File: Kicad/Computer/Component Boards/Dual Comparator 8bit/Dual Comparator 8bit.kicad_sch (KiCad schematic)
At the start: 12 parts, among them IC1 SN74F521NSR, IC2 74LVC16373ADL,118, IC3 SN74F521NSR, IC5 AP7365-33WG-7, J2 Conn_02x20_Counter_Clockwise

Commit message: Routed (mostly) the Dual 8bit comparator.
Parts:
- removed C5: 1μF, SamacSys_Parts:C_0805, symbol HCP65:C_0805
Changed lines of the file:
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@@
     (effects (font (size 1.27 1.27)) (justify right bottom))
-  )
-  (label "GND" (at 168.91 154.305 0) (fields_autoplaced)
-    (effects (font (size 1.27 1.27)) (justify left bottom))
   )
   (label "GND" (at 104.14 113.665 180) (fields_autoplaced)
@@
   )
   (label "D5" (at 40.64 130.81 180) (fields_autoplaced)
-    (effects (font (size 1.27 1.27)) (justify right bottom))
-  )
-  (label "3.3V" (at 163.83 154.305 180) (fields_autoplaced)
     (effects (font (size 1.27 1.27)) (justify right bottom))
   )
@@
         )
       )
-      (project "Pico Sound"
-        (path "/36ae9fab-3bd5-422b-bccc-b7d474dd236c"
-          (reference "C23") (unit 1)
-        )
-      )
-      (project "Video Timer"
-        (path "/5ce90b85-49a2-4937-86c7-662b0d6f8431"
-          (reference "C?") (unit 1)
-        )
-        (path "/5ce90b85-49a2-4937-86c7-662b0d6f8431/662feba9-2017-4e89-b774-f7d895f327d7"
-          (reference "C42") (unit 1)
-        )
-      )
-      (project "Sound"
-        (path "/8357857d-ab8c-4646-b786-aad4001c0a6b/f77e925c-a0a2-46fc-a442-a4077818f930"
-          (reference "C52") (unit 1)
-        )
-      )
-    )
-  )
-  (symbol (lib_id "HCP65:C_0805") (at 163.83 154.305 0) (unit 1)
-    (in_bom yes) (on_board yes) (dnp no)
-    (property "Reference" "C5" (at 166.116 151.765 0)
-      (effects (font (size 1.27 1.27)))
-    )
-    (property "Value" "1μF" (at 166.37 156.845 0)
-      (effects (font (size 1.27 1.27)))
-    )
-    (property "Footprint" "SamacSys_Parts:C_0805" (at 180.594 161.925 0)
-      (effects (font (size 1.27 1.27)) hide)
-    )
-    (property "Datasheet" "" (at 166.0525 153.9875 90)
-      (effects (font (size 1.27 1.27)) hide)
-    )
-    (pin "1")
-    (pin "2")
-    (instances
-      (project "Dual Comparator 8bit"
-        (path "/337b5f72-8be1-4121-9dc6-479b565482b2"
-          (reference "C5") (unit 1)
-        )
-      )

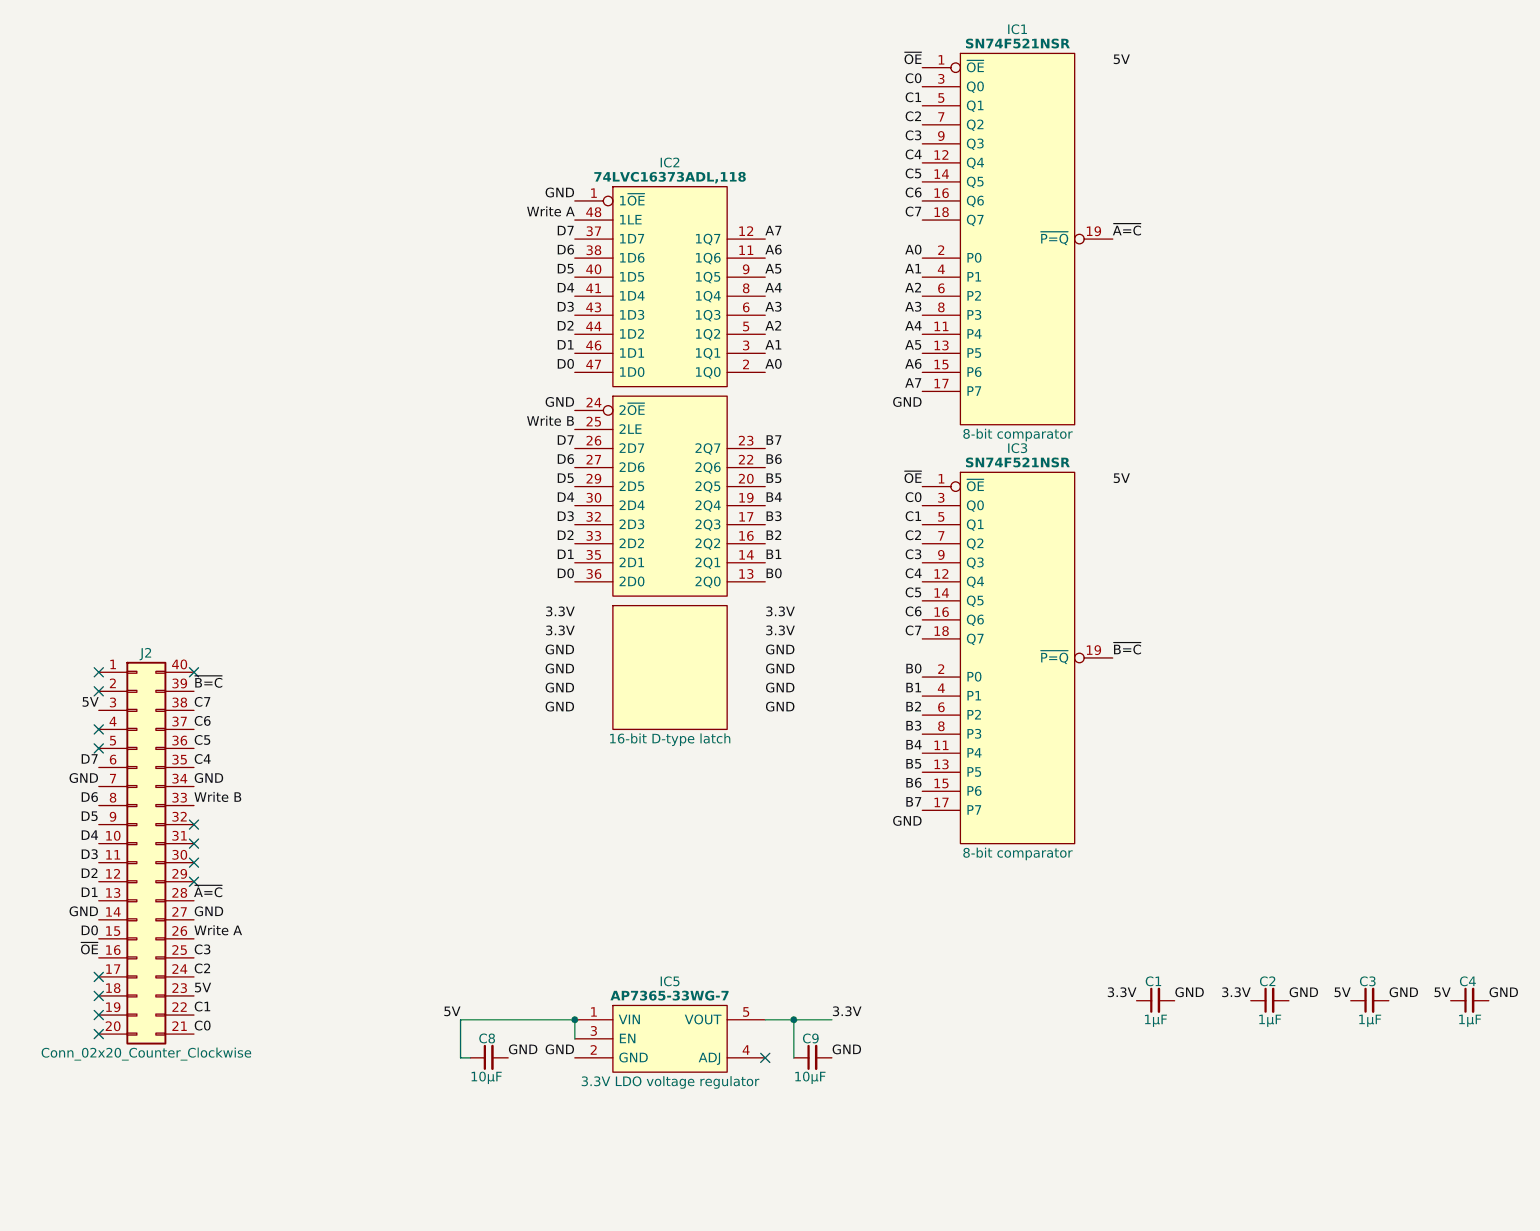
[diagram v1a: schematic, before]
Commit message: Added terminal count output and latch enable to 16bit and 24bit counters.
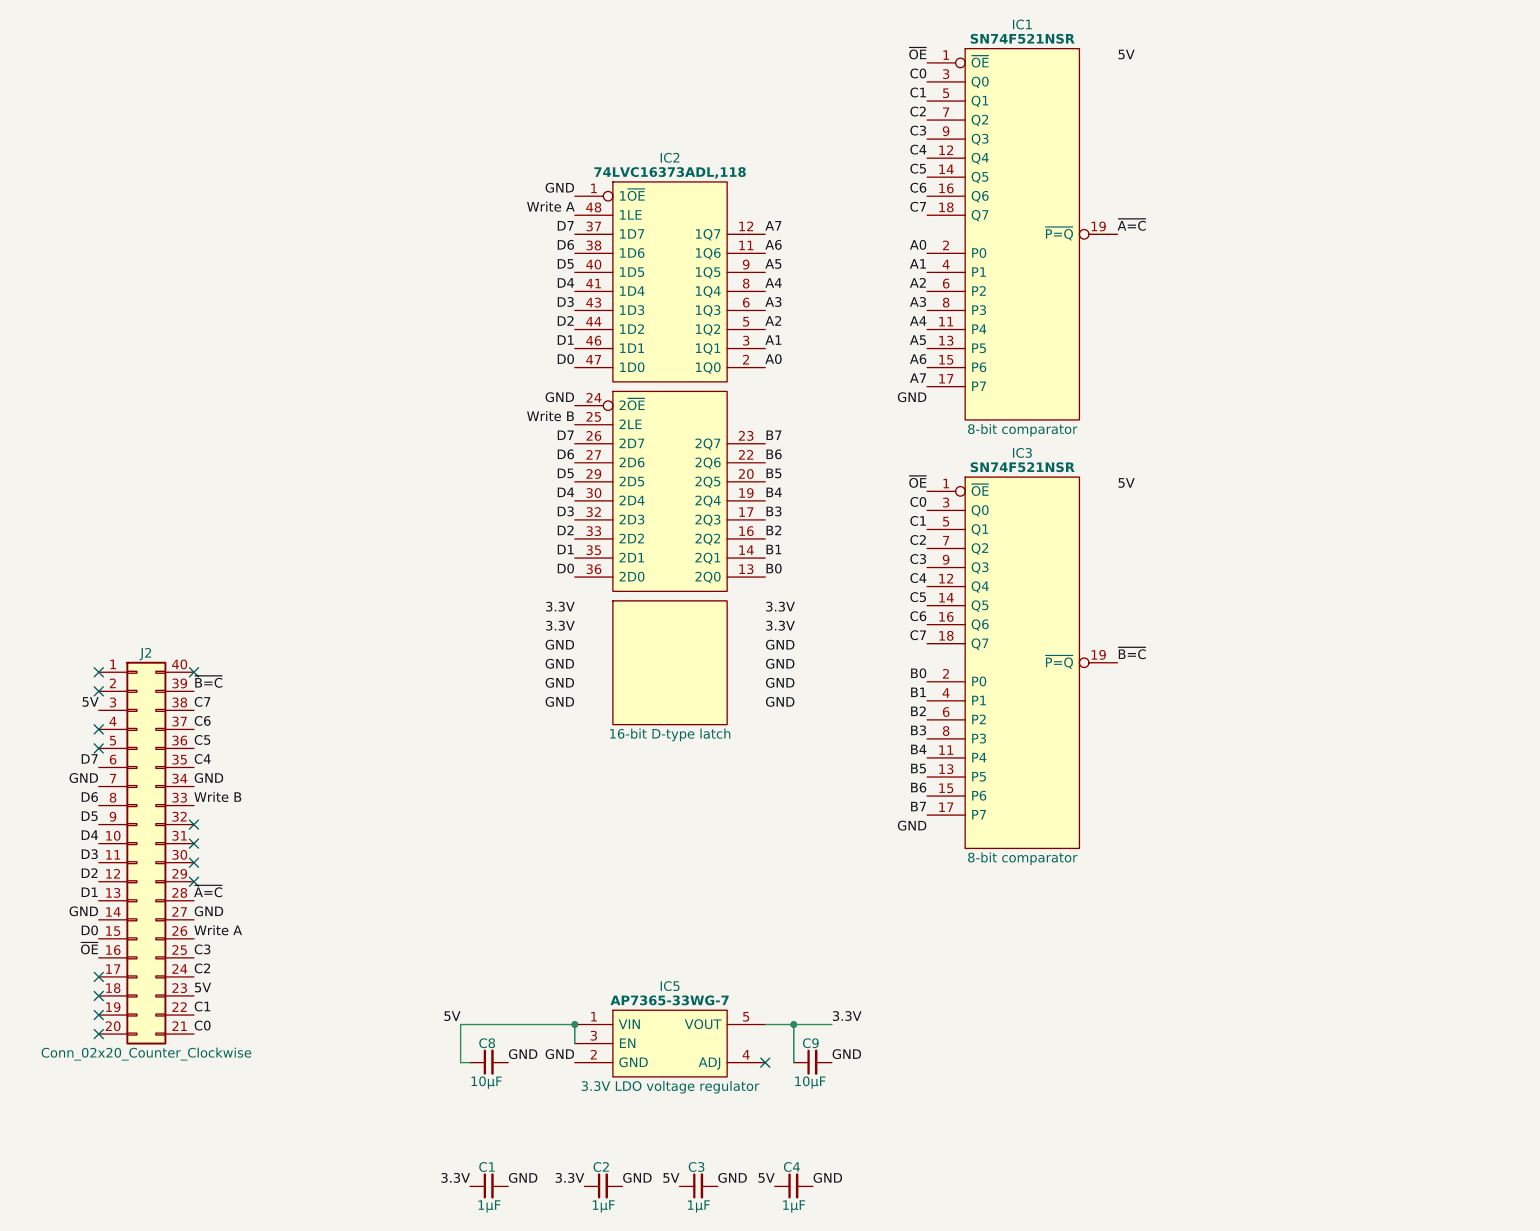
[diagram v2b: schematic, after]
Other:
- moved on the sheet: C1, C2, C3, C4, C8, C9, IC1, IC2, IC3, IC5

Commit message: Regenerating some gerbers again with paste layers.
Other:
- title: 24bit Counter with 8bit data IO -> Dual 8bit Comparator
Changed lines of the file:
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@@
   (paper "A4")
   (title_block
-    (title "24bit Counter with 8bit data IO")
+    (title "Dual 8bit Comparator")
     (date "2023-10-07")
     (rev "V0")

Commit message: Removed some component copper fills.
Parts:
- IC1, IC3: footprint SOIC127P780X200-20N -> SamacSys_Parts:SOIC127P780X200-20N; Garbage (none) -> 8-Bit Identity/Magnitude Comparators (P=Q) with Enable
- IC2: footprint SOP64P1025X280-48N -> SamacSys_Parts:SOP64P1025X280-48N; Garbage (none) -> 74LVC16373A; 74LVCH16373A - 16-bit D-type transparent latch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
- IC5: footprint SOT95P285X130-5N -> SamacSys_Parts:SOT95P285X130-5N

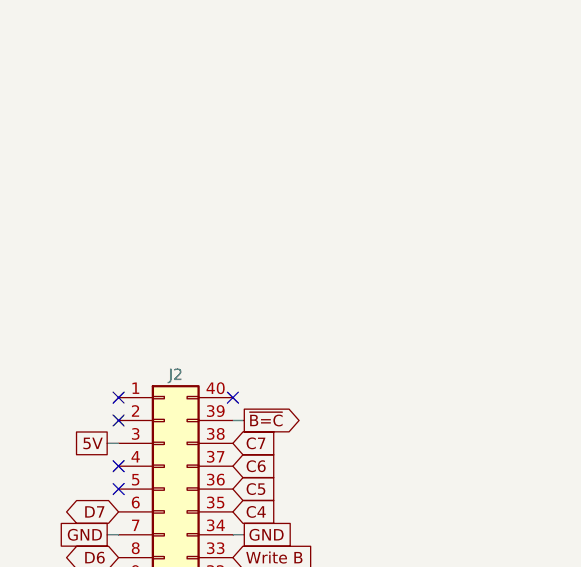
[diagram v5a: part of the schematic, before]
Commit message: Use VRML instead of STEPs for Graphics Board models.
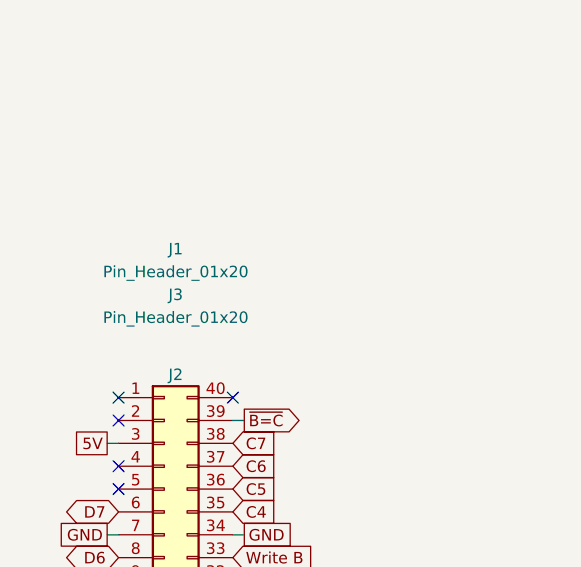
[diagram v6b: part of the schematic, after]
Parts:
- added J1, J3: Pin_Header_01x20, SamacSys_Parts:PinHeader_1x20_P2.54mm_Vertical, symbol HCP65:Pin_Header_01x32
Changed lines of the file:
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@@
+	)
+	(symbol
+		(lib_id "HCP65:Pin_Header_01x32")
+		(at 46.99 100.33 0)
+		(unit 1)
+		(exclude_from_sim no)
+		(in_bom yes)
+		(on_board yes)
+		(dnp no)
+		(property "Reference" "J3"
+			(at 46.99 99.06 0)
+			(effects
+				(font
+					(size 1.27 1.27)
+				)
+			)
+		)
+		(property "Value" "Pin_Header_01x20"
+			(at 46.99 101.6 0)
+			(effects
+				(font
+					(size 1.27 1.27)
+				)
+			)
+		)
+		(property "Footprint" "SamacSys_Parts:PinHeader_1x20_P2.54mm_Vertical"
+			(at 46.99 104.14 0)
+			(effects
+				(font
+					(size 1.27 1.27)
+				)
+				(hide yes)
+			)
+		)
+		(property "Datasheet" "~"
+			(at 41.91 100.33 0)
+			(effects
+				(font
+					(size 1.27 1.27)
+				)
+				(hide yes)
+			)
+		)
+		(property "Description" ""
+			(at 46.99 100.33 0)
+			(effects
+				(font
+					(size 1.27 1.27)
+				)
+				(hide yes)
+			)
+		)
+		(instances
+			(project "Dual Comparator 8bit"
+				(path "/337b5f72-8be1-4121-9dc6-479b565482b2"
+					(reference "J3")
+					(unit 1)
+				)
+			)
+		)
 	)
 	(symbol
@@
 					(unit 1)
 				)
+			)
+		)
+	)
+	(symbol
+		(lib_id "HCP65:Pin_Header_01x32")
+		(at 46.99 95.25 0)
+		(mirror y)
+		(unit 1)
+		(exclude_from_sim no)
+		(in_bom yes)
+		(on_board yes)
+		(dnp no)
+		(property "Reference" "J1"
+			(at 46.99 93.98 0)
+			(effects
+				(font
+					(size 1.27 1.27)
+				)
+			)
+		)
+		(property "Value" "Pin_Header_01x20"
+			(at 46.99 96.52 0)
+			(effects
+				(font
+					(size 1.27 1.27)
+				)
+			)
+		)
+		(property "Footprint" "SamacSys_Parts:PinHeader_1x20_P2.54mm_Vertical"
+			(at 46.99 99.06 0)
+			(effects
+				(font
+					(size 1.27 1.27)
+				)
+				(hide yes)
+			)
+		)
+		(property "Datasheet" "~"
+			(at 52.07 95.25 0)
+			(effects
+				(font
+					(size 1.27 1.27)
+				)
+				(hide yes)
+			)
+		)
+		(property "Description" ""
+			(at 46.99 95.25 0)
+			(effects
+				(font
+					(size 1.27 1.27)
+				)
+				(hide yes)
+			)
+		)
+		(instances
+			(project "Dual Comparator 8bit"
+				(path "/337b5f72-8be1-4121-9dc6-479b565482b2"
+					(reference "J1")
+					(unit 1)
+				)

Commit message: Rounded Dual Comparator 8bit traces.
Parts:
- IC1, IC3: Garbage 8-Bit Identity/Magnitude Comparators (P=Q) with Enable -> (none)
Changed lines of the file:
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@@
-			)
-		)
-		(property "Garbage" "8-Bit Identity/Magnitude Comparators (P=Q) with Enable"
-			(at 151.13 86.36 0)
-			(effects
-				(font
-					(size 1.27 1.27)
-				)
-				(hide yes)
 			)
 		)
@@
 			(effects
 				(font
-					(size 1.27 1.27)
-				)
-				(hide yes)
-			)
-		)
-		(property "Garbage" "8-Bit Identity/Magnitude Comparators (P=Q) with Enable"
-			(at 151.13 29.21 0)
-			(effects
-				(font
